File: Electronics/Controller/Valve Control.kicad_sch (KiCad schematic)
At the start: 2 parts, among them J20 FRONT HEIGHT, J21 REAR HEIGHT

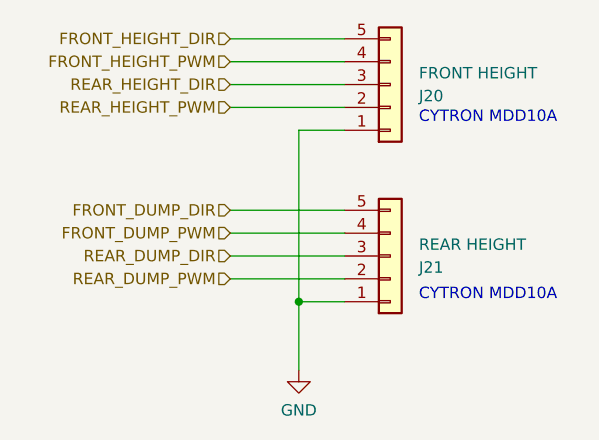
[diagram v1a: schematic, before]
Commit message: Working on controller case. Updated labels for valve controls on controller schematic.
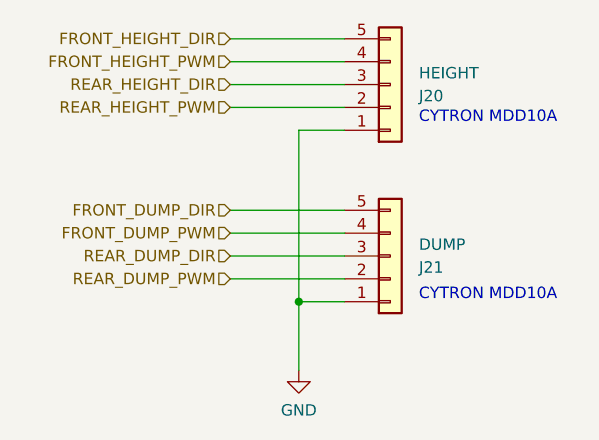
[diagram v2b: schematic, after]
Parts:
- J20: value FRONT HEIGHT -> HEIGHT
- J21: value REAR HEIGHT -> DUMP
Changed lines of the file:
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@@
       (effects (font (size 1.27 1.27)) (justify left))
     )
-    (property "Value" "FRONT HEIGHT" (at 155.575 82.55 0)
+    (property "Value" "HEIGHT" (at 155.575 82.55 0)
       (effects (font (size 1.27 1.27)) (justify left))
     )
@@
       (effects (font (size 1.27 1.27)) (justify left))
     )
-    (property "Value" "REAR HEIGHT" (at 155.575 101.6 0)
+    (property "Value" "DUMP" (at 155.575 101.6 0)
       (effects (font (size 1.27 1.27)) (justify left))
     )
